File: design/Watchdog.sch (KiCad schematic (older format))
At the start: 25 parts, among them U401 74LV14, U402 74LVC2G00, U403 STWD100xxWY, U404 STWD100xxWY, U405 74AHC157

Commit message: Simplify Watchdog
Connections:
- net IN_CHARGE: now also U402.1; no longer U402.5
- net FC2_WDO: now reaches U404.1 (~WDO)
- net FC2_WDO: now also U402.6; no longer U402.6
- net FC1_WDO: now reaches U403.1 (~WDO)
- net FC1_WDO: now also U402.2; no longer U402.1
- net at R407.1: now also U402.3; no longer U402.7
- new net: U402.5, U402.7
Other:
- moved on the sheet: C406, R401, R407, TP401, U403
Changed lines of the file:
@@
 $Comp
 L CommsCard:74LVC2G00 U402
-U 2 1 5A7B6676
-P 6100 3200
-F 0 "U402" H 6075 3467 50  0000 C CNN
-F 1 "74LVC2G00" H 6075 3376 50  0000 C CNN
-F 2 "Package_SO:VSSOP-8_2.3x2mm_P0.5mm" H 6100 3200 50  0001 C CNN
-F 3 "http://www.ti.com/lit/ds/symlink/sn74lvc2g00.pdf" H 6100 3200 50  0001 C CNN
-F 4 "SN74LVC2G00DCUR" H 6100 3200 50  0001 C CNN "mpn"
-	2    6100 3200
-	1    0    0    -1
-$EndComp
-Wire Wire Line
-	5800 3150 5750 3150
-Wire Wire Line
-	7050 1900 6700 1900
-Wire Wire Line
-	6350 3200 6550 3200
-Wire Wire Line
-	6550 3200 6550 3450
-Wire Wire Line
-	6550 3450 5600 3450
-Wire Wire Line
-	5600 3450 5600 1950
-Wire Wire Line
-	5600 1950 5800 1950
-Wire Wire Line
-	6400 1900 6350 1900
-Wire Wire Line
-	5750 2600 7050 2600
-Wire Wire Line
-	5750 2600 5750 3150
-Wire Wire Line
-	7050 1900 7050 2600
-Wire Wire Line
-	5800 3250 4800 3250
-Wire Wire Line
-	5800 1850 4750 1850
+U 1 1 5A7B6676
+P 6050 1850
+F 0 "U402" H 6025 2117 50  0000 C CNN
+F 1 "74LVC2G00" H 6025 2026 50  0000 C CNN
+F 2 "Package_SO:VSSOP-8_2.3x2mm_P0.5mm" H 6050 1850 50  0001 C CNN
+F 3 "http://www.ti.com/lit/ds/symlink/sn74lvc2g00.pdf" H 6050 1850 50  0001 C CNN
+F 4 "SN74LVC2G00DCUR" H 6050 1850 50  0001 C CNN "mpn"
+	1    6050 1850
+	1    0    0    -1
+$EndComp
+Wire Wire Line
+	7400 1900 7350 1900
+Wire Wire Line
+	7050 1900 7000 1900
+Wire Wire Line
+	7400 1900 7400 2600
 $Comp
 L power:GND #PWR0407
 U 1 1 5A7B7021
-P 4400 2250
-F 0 "#PWR0407" H 4400 2000 50  0001 C CNN
-F 1 "GND" H 4405 2077 50  0000 C CNN
-F 2 "" H 4400 2250 50  0001 C CNN
-F 3 "" H 4400 2250 50  0001 C CNN
-	1    4400 2250
-	1    0    0    -1
-$EndComp
-Wire Wire Line
-	4400 2250 4400 2200
+P 4400 2300
+F 0 "#PWR0407" H 4400 2050 50  0001 C CNN
+F 1 "GND" H 4405 2127 50  0000 C CNN
+F 2 "" H 4400 2300 50  0001 C CNN
+F 3 "" H 4400 2300 50  0001 C CNN
+	1    4400 2300
+	1    0    0    -1
+$EndComp
+Wire Wire Line
+	4400 2300 4400 2250
 $Comp
 L power:GND #PWR0409
@@
 $Comp
 L CommsCard:74LVC2G00 U402
-U 1 1 5A7B74F5
-P 6100 1900
-F 0 "U402" H 6075 2167 50  0000 C CNN
-F 1 "74LVC2G00" H 6075 2076 50  0000 C CNN
-F 2 "Package_SO:VSSOP-8_2.3x2mm_P0.5mm" H 6100 1900 50  0001 C CNN
-F 3 "http://www.ti.com/lit/ds/symlink/sn74lvc2g00.pdf" H 6100 1900 50  0001 C CNN
-F 4 "SN74LVC2G00DCUR" H 6100 1900 50  0001 C CNN "mpn"
-	1    6100 1900
-	1    0    0    -1
-$EndComp
-Wire Wire Line
-	4050 1750 3800 1750
-Text HLabel 3700 1750 0    50   Input ~ 0
+U 2 1 5A7B74F5
+P 6750 1900
+F 0 "U402" H 6725 2167 50  0000 C CNN
+F 1 "74LVC2G00" H 6725 2076 50  0000 C CNN
+F 2 "Package_SO:VSSOP-8_2.3x2mm_P0.5mm" H 6750 1900 50  0001 C CNN
+F 3 "http://www.ti.com/lit/ds/symlink/sn74lvc2g00.pdf" H 6750 1900 50  0001 C CNN
+F 4 "SN74LVC2G00DCUR" H 6750 1900 50  0001 C CNN "mpn"
+	2    6750 1900
+	1    0    0    -1
+$EndComp
+Wire Wire Line
+	4050 1800 3800 1800
+Text HLabel 3700 1800 0    50   Input ~ 0
 FC1_WD
 $Comp
 L Connector_Specialized:Test_Point TP401
 U 1 1 5A7B77EA
-P 3800 1500
-F 0 "TP401" H 3858 1620 50  0000 L CNN
-F 1 "Test_Point" H 3858 1529 50  0000 L CNN
-F 2 "TestPoint:TestPoint_Pad_D1.5mm" H 4000 1500 50  0001 C CNN
-F 3 "~" H 4000 1500 50  0001 C CNN
-F 4 "~" H 3800 1500 50  0001 C CNN "mpn"
-	1    3800 1500
-	1    0    0    -1
-$EndComp
-Wire Wire Line
-	3800 1750 3800 1500
-Connection ~ 3800 1750
-Wire Wire Line
-	3800 1750 3700 1750
+P 3800 1550
+F 0 "TP401" H 3858 1670 50  0000 L CNN
+F 1 "Test_Point" H 3858 1579 50  0000 L CNN
+F 2 "TestPoint:TestPoint_Pad_D1.5mm" H 4000 1550 50  0001 C CNN
+F 3 "~" H 4000 1550 50  0001 C CNN
+F 4 "~" H 3800 1550 50  0001 C CNN "mpn"
+	1    3800 1550
+	1    0    0    -1
+$EndComp
+Wire Wire Line
+	3800 1800 3800 1550
+Connection ~ 3800 1800
+Wire Wire Line
+	3800 1800 3700 1800
 Wire Wire Line
 	4100 3150 3850 3150
@@
 ~FC2_PWREN
 Wire Wire Line
-	3050 1950 3050 1900
-Wire Wire Line
-	3050 1950 4050 1950
+	3050 2000 3050 1950
+Wire Wire Line
+	3050 2000 4050 2000
 $Comp
 L power:+3V3 #PWR0401
 U 1 1 5A7B889A
-P 3050 1550
-F 0 "#PWR0401" H 3050 1400 50  0001 C CNN
-F 1 "+3V3" H 3065 1723 50  0000 C CNN
-F 2 "" H 3050 1550 50  0001 C CNN
-F 3 "" H 3050 1550 50  0001 C CNN
-	1    3050 1550
-	1    0    0    -1
-$EndComp
-Wire Wire Line
-	3050 1600 3050 1550
-Text HLabel 3050 1950 0    50   Input ~ 0
+P 3050 1600
+F 0 "#PWR0401" H 3050 1450 50  0001 C CNN
+F 1 "+3V3" H 3065 1773 50  0000 C CNN
+F 2 "" H 3050 1600 50  0001 C CNN
+F 3 "" H 3050 1600 50  0001 C CNN
+	1    3050 1600
+	1    0    0    -1
+$EndComp
+Wire Wire Line
+	3050 1650 3050 1600
+Text HLabel 3050 2000 0    50   Input ~ 0
 ~FC1_PWREN
 $Comp
@@
 L power:+3V3 #PWR0406
 U 1 1 5A7B9130
-P 4400 1500
-F 0 "#PWR0406" H 4400 1350 50  0001 C CNN
-F 1 "+3V3" H 4415 1673 50  0000 C CNN
-F 2 "" H 4400 1500 50  0001 C CNN
-F 3 "" H 4400 1500 50  0001 C CNN
-	1    4400 1500
+P 4400 1550
+F 0 "#PWR0406" H 4400 1400 50  0001 C CNN
+F 1 "+3V3" H 4415 1723 50  0000 C CNN
+F 2 "" H 4400 1550 50  0001 C CNN
+F 3 "" H 4400 1550 50  0001 C CNN
+	1    4400 1550
 	1    0    0    -1
 $EndComp
@@
 	1    0    0    -1
 $EndComp
-Connection ~ 7050 2600
+Connection ~ 7400 2600
 $Comp
 L power:+3V3 #PWR0412
@@
 L CommsCard:STWD100xxWY U403
 U 1 1 5A7BE12B
-P 4400 1850
-F 0 "U403" H 4791 1896 50  0000 L CNN
-F 1 "STWD100xxWY" H 4791 1805 50  0000 L CNN
-F 2 "Package_TO_SOT_SMD:SOT-353_SC-70-5" H 4450 2050 50  0001 C CNN
-F 3 "http://www.st.com/content/ccc/resource/technical/document/datasheet/06/6a/b3/83/9a/c7/4f/22/CD00176077.pdf/files/CD00176077.pdf/jcr:content/translations/en.CD00176077.pdf" H 4550 2150 50  0001 C CNN
-F 4 "STWD100PYW83F" H 4400 1850 50  0001 C CNN "mpn"
-	1    4400 1850
+P 4400 1900
+F 0 "U403" H 4791 1946 50  0000 L CNN
+F 1 "STWD100xxWY" H 4791 1855 50  0000 L CNN
+F 2 "Package_TO_SOT_SMD:SOT-353_SC-70-5" H 4450 2100 50  0001 C CNN
+F 3 "http://www.st.com/content/ccc/resource/technical/document/datasheet/06/6a/b3/83/9a/c7/4f/22/CD00176077.pdf/files/CD00176077.pdf/jcr:content/translations/en.CD00176077.pdf" H 4550 2200 50  0001 C CNN
+F 4 "STWD100PYW83F" H 4400 1900 50  0001 C CNN "mpn"
+	1    4400 1900
 	1    0    0    -1
 $EndComp
@@
 Connection ~ 8650 3050
 Wire Wire Line
-	7050 2600 7050 2850
-Wire Wire Line
-	7050 2850 7300 2850
-Text HLabel 7300 2850 2    50   Output ~ 0
+	7400 2600 7400 2850
+Wire Wire Line
+	7400 2850 7650 2850
+Text HLabel 7650 2850 2    50   Output ~ 0
 IN_CHARGE
 $Comp
@@
 L Device:R R407
 U 1 1 5A836CA1
-P 6550 1900
-F 0 "R407" H 6480 1854 50  0000 R CNN
-F 1 "10k" H 6480 1945 50  0000 R CNN
-F 2 "Resistor_SMD:R_0603_1608Metric" V 6480 1900 50  0001 C CNN
-F 3 "http://www.te.com/commerce/DocumentDelivery/DDEController?Action=srchrtrv&DocNm=1773204&DocType=DS&DocLang=English" H 6550 1900 50  0001 C CNN
-F 4 "CRG0603J10K" H 6550 1900 50  0001 C CNN "mpn"
-	1    6550 1900
+P 7200 1900
+F 0 "R407" H 7130 1854 50  0000 R CNN
+F 1 "10k" H 7130 1945 50  0000 R CNN
+F 2 "Resistor_SMD:R_0603_1608Metric" V 7130 1900 50  0001 C CNN
+F 3 "http://www.te.com/commerce/DocumentDelivery/DDEController?Action=srchrtrv&DocNm=1773204&DocType=DS&DocLang=English" H 7200 1900 50  0001 C CNN
+F 4 "CRG0603J10K" H 7200 1900 50  0001 C CNN "mpn"
+	1    7200 1900
 	0    -1   1    0
 $EndComp
@@
 L Device:R R401
 U 1 1 5A83892F
-P 3050 1750
-F 0 "R401" H 2980 1704 50  0000 R CNN
-F 1 "10k" H 2980 1795 50  0000 R CNN
-F 2 "Resistor_SMD:R_0603_1608Metric" V 2980 1750 50  0001 C CNN
-F 3 "http://www.te.com/commerce/DocumentDelivery/DDEController?Action=srchrtrv&DocNm=1773204&DocType=DS&DocLang=English" H 3050 1750 50  0001 C CNN
-F 4 "CRG0603J10K" H 3050 1750 50  0001 C CNN "mpn"
-	1    3050 1750
+P 3050 1800
+F 0 "R401" H 2980 1754 50  0000 R CNN
+F 1 "10k" H 2980 1845 50  0000 R CNN
+F 2 "Resistor_SMD:R_0603_1608Metric" V 2980 1800 50  0001 C CNN
+F 3 "http://www.te.com/commerce/DocumentDelivery/DDEController?Action=srchrtrv&DocNm=1773204&DocType=DS&DocLang=English" H 3050 1800 50  0001 C CNN
+F 4 "CRG0603J10K" H 3050 1800 50  0001 C CNN "mpn"
+	1    3050 1800
 	1    0    0    1
 $EndComp
@@
 L Device:C C406
 U 1 1 5A887245
-P 7050 3150
-F 0 "C406" H 7165 3196 50  0000 L CNN
-F 1 "0u1F" H 7165 3105 50  0000 L CNN
-F 2 "Capacitor_SMD:C_0603_1608Metric" H 7088 3000 50  0001 C CNN
-F 3 "http://www.samsungsem.com/kr/support/product-search/mlcc/CL10B104KO8WPNC.jsp" H 7050 3150 50  0001 C CNN
-F 4 "CL10B104KO8WPNC" H 7050 3150 50  0001 C CNN "mpn"
-	1    7050 3150
+P 7400 3150
+F 0 "C406" H 7515 3196 50  0000 L CNN
+F 1 "0u1F" H 7515 3105 50  0000 L CNN
+F 2 "Capacitor_SMD:C_0603_1608Metric" H 7438 3000 50  0001 C CNN
+F 3 "http://www.samsungsem.com/kr/support/product-search/mlcc/CL10B104KO8WPNC.jsp" H 7400 3150 50  0001 C CNN
+F 4 "CL10B104KO8WPNC" H 7400 3150 50  0001 C CNN "mpn"
+	1    7400 3150
 	1    0    0    -1
 $EndComp
@@
 L power:GND #PWR0411
 U 1 1 5A88736C
-P 7050 3350
-F 0 "#PWR0411" H 7050 3100 50  0001 C CNN
-F 1 "GND" H 7055 3177 50  0000 C CNN
-F 2 "" H 7050 3350 50  0001 C CNN
-F 3 "" H 7050 3350 50  0001 C CNN
-	1    7050 3350
-	1    0    0    -1
-$EndComp
-Wire Wire Line
-	7050 3350 7050 3300
-Connection ~ 7050 2850
-Wire Wire Line
-	7050 2850 7050 3000
+P 7400 3350
+F 0 "#PWR0411" H 7400 3100 50  0001 C CNN
+F 1 "GND" H 7405 3177 50  0000 C CNN
+F 2 "" H 7400 3350 50  0001 C CNN
+F 3 "" H 7400 3350 50  0001 C CNN
+	1    7400 3350
+	1    0    0    -1
+$EndComp
+Wire Wire Line
+	7400 3350 7400 3300
+Connection ~ 7400 2850
+Wire Wire Line
+	7400 2850 7400 3000
 Connection ~ 9900 5600
 Wire Wire Line
-	7050 2600 8250 2600
+	7400 2600 8250 2600
 Wire Wire Line
 	9900 5600 9900 5500
+Text Label 5150 3250 0    50   ~ 0
+FC2_WDO
+Text Label 5200 1900 0    50   ~ 0
+FC1_WDO
+Wire Wire Line
+	4750 1900 5750 1900
+Wire Wire Line
+	7400 1900 7400 1400
+Wire Wire Line
+	7400 1400 5650 1400
+Wire Wire Line
+	5650 1400 5650 1800
+Wire Wire Line
+	5650 1800 5750 1800
+Connection ~ 7400 1900
+Wire Wire Line
+	6450 1850 6300 1850
+Wire Wire Line
+	6350 3250 6350 1950
+Wire Wire Line
+	4800 3250 6350 3250
+Wire Wire Line
+	6350 1950 6450 1950
+Connection ~ 6150 2800
 $EndSCHEMATC

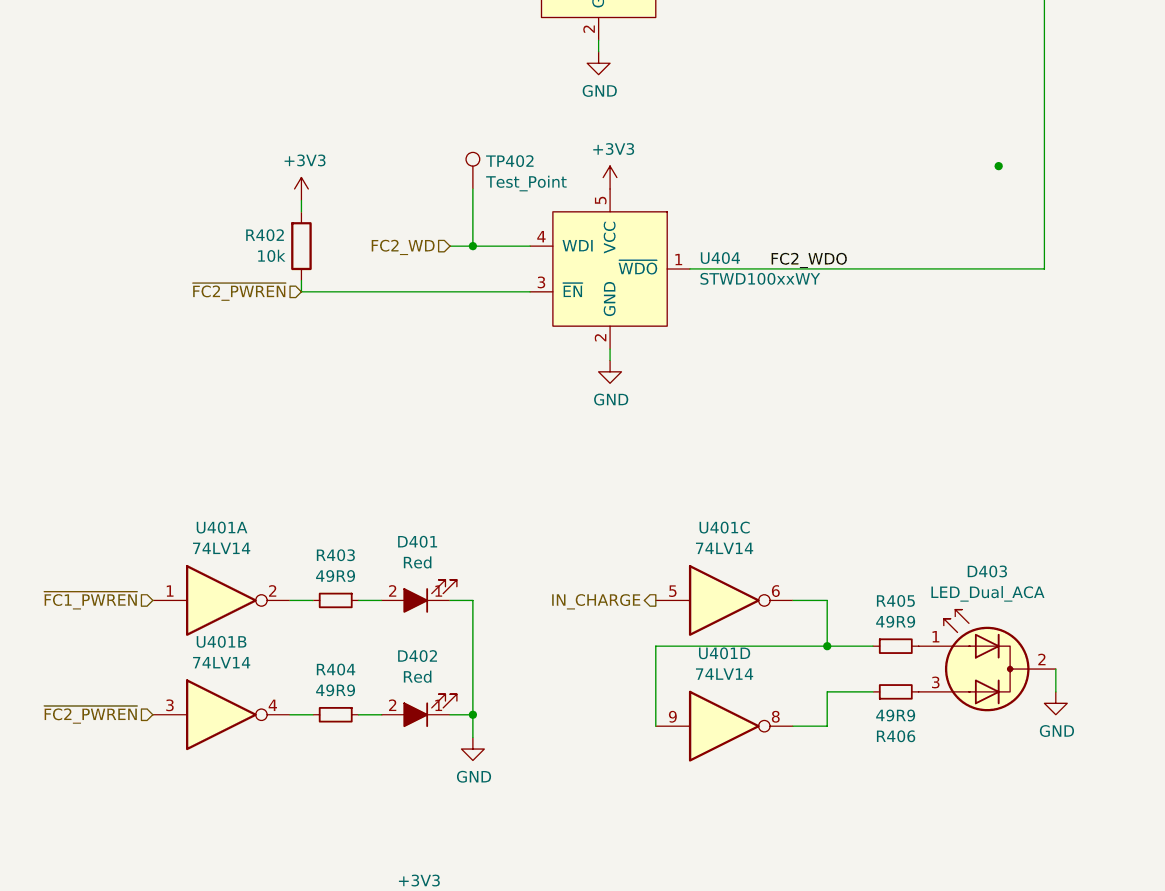
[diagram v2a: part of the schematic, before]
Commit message: Layout additional watchdog
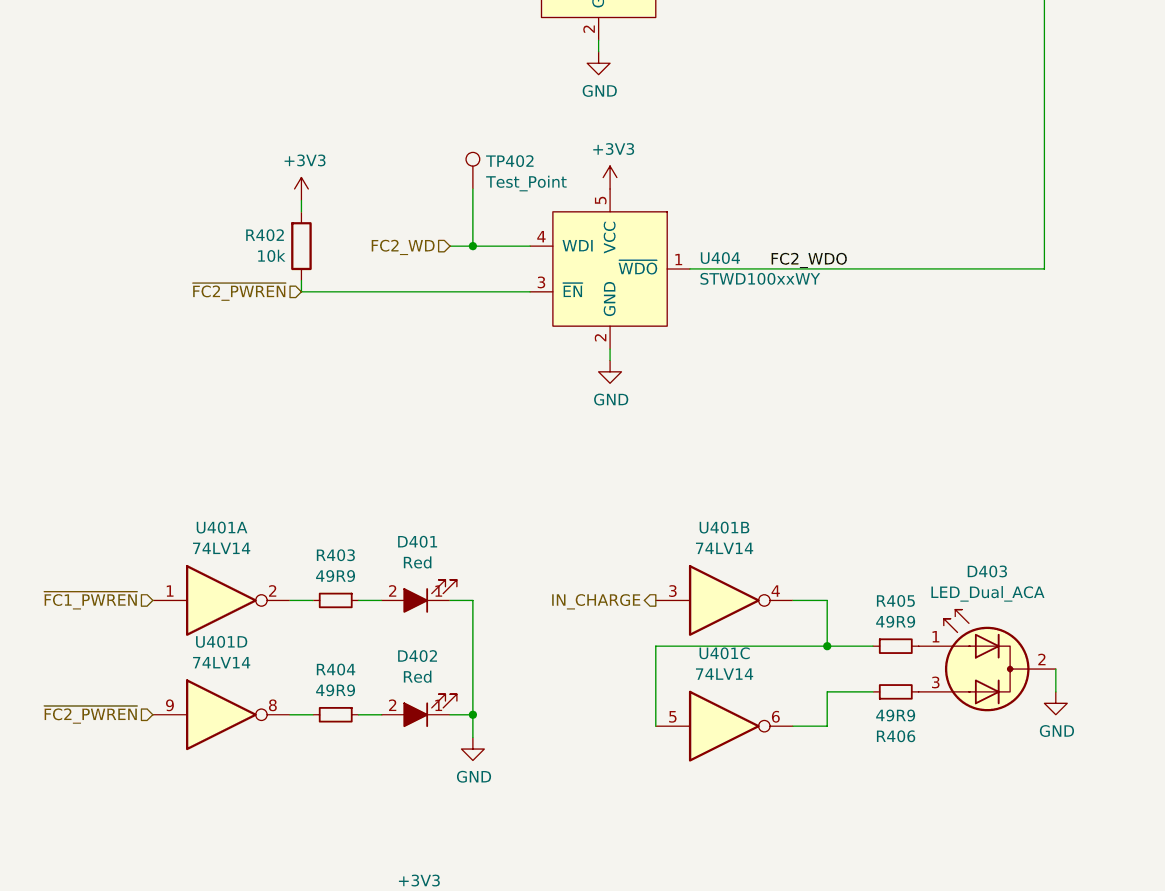
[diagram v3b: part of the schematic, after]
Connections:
- net IN_CHARGE: now also U401.3; no longer U401.5
- net ~FC2_PWREN: now also U401.9; no longer U401.3
- net at U401.4: now also R405.1, U401.5; no longer R404.2
- net at R406.1: now also U401.6; no longer U401.8
- new net: R404.2, U401.8
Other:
- moved on the sheet: U401B, U401C, U401D
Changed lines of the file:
@@
 L Logic_74xx:74HC04 U401
 U 3 1 5A8462FD
-P 4950 4700
-F 0 "U401" H 4950 5017 50  0000 C CNN
-F 1 "74LV14" H 4950 4926 50  0000 C CNN
-F 2 "Package_SO:TSSOP-14_4.4x5mm_P0.65mm" H 4950 4700 50  0001 C CNN
-F 3 "http://www.ti.com/lit/ds/symlink/sn74lv14a.pdf" H 4950 4700 50  0001 C CNN
-F 4 "SN74LV14APWR" H 4950 4700 50  0001 C CNN "mpn"
-	3    4950 4700
+P 4950 5250
+F 0 "U401" H 4950 5567 50  0000 C CNN
+F 1 "74LV14" H 4950 5476 50  0000 C CNN
+F 2 "Package_SO:TSSOP-14_4.4x5mm_P0.65mm" H 4950 5250 50  0001 C CNN
+F 3 "http://www.ti.com/lit/ds/symlink/sn74lv14a.pdf" H 4950 5250 50  0001 C CNN
+F 4 "SN74LV14APWR" H 4950 5250 50  0001 C CNN "mpn"
+	3    4950 5250
 	1    0    0    -1
 $EndComp
@@
 L Logic_74xx:74HC04 U401
 U 4 1 5A85B128
-P 4950 5250
-F 0 "U401" H 4950 5567 50  0000 C CNN
-F 1 "74LV14" H 4950 5476 50  0000 C CNN
-F 2 "Package_SO:TSSOP-14_4.4x5mm_P0.65mm" H 4950 5250 50  0001 C CNN
-F 3 "http://www.ti.com/lit/ds/symlink/sn74lv14a.pdf" H 4950 5250 50  0001 C CNN
-F 4 "SN74LV14APWR" H 4950 5250 50  0001 C CNN "mpn"
-	4    4950 5250
-	1    0    0    -1
-$EndComp
-$Comp
-L Logic_74xx:74HC04 U401
-U 2 1 5A85B182
 P 2750 5200
 F 0 "U401" H 2750 5517 50  0000 C CNN
@@
 F 3 "http://www.ti.com/lit/ds/symlink/sn74lv14a.pdf" H 2750 5200 50  0001 C CNN
 F 4 "SN74LV14APWR" H 2750 5200 50  0001 C CNN "mpn"
-	2    2750 5200
+	4    2750 5200
+	1    0    0    -1
+$EndComp
+$Comp
+L Logic_74xx:74HC04 U401
+U 2 1 5A85B182
+P 4950 4700
+F 0 "U401" H 4950 5017 50  0000 C CNN
+F 1 "74LV14" H 4950 4926 50  0000 C CNN
+F 2 "Package_SO:TSSOP-14_4.4x5mm_P0.65mm" H 4950 4700 50  0001 C CNN
+F 3 "http://www.ti.com/lit/ds/symlink/sn74lv14a.pdf" H 4950 4700 50  0001 C CNN
+F 4 "SN74LV14APWR" H 4950 4700 50  0001 C CNN "mpn"
+	2    4950 4700
 	1    0    0    -1
 $EndComp
@@
 Wire Wire Line
 	6350 1950 6450 1950
-Connection ~ 6150 2800
 $EndSCHEMATC

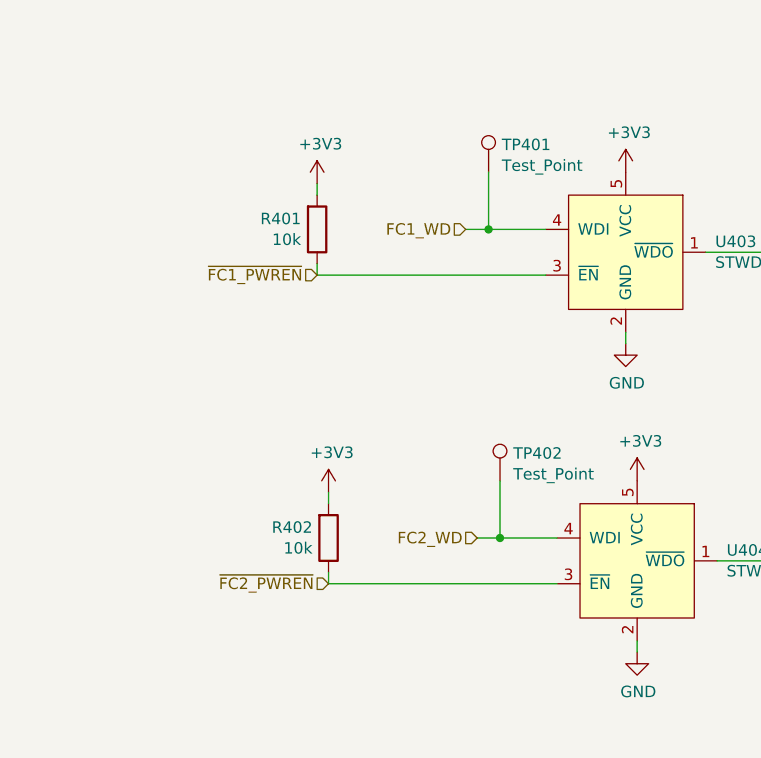
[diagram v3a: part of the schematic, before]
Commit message: Further LOS updates.  Compressing space
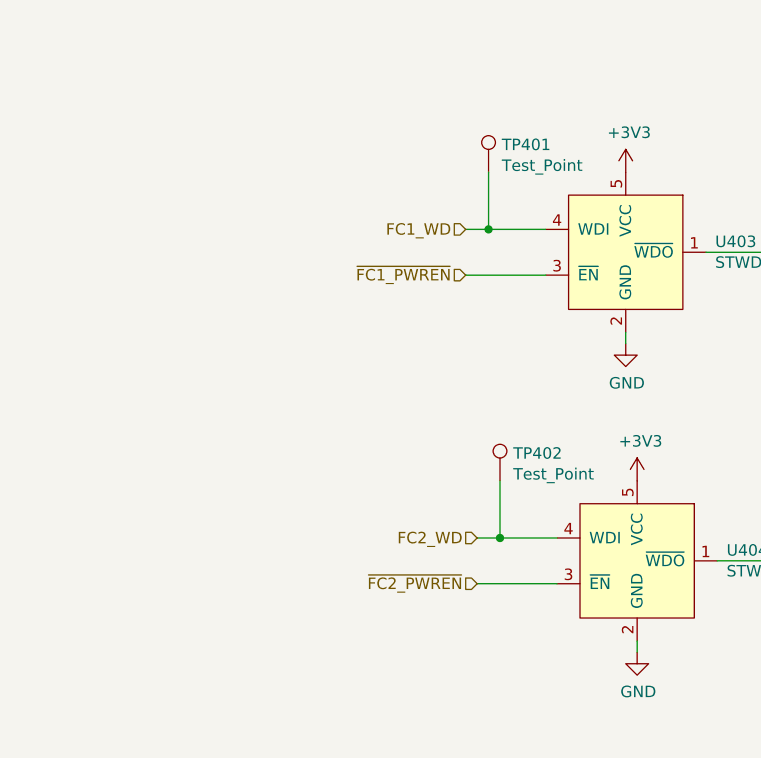
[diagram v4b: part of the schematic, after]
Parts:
- removed R401, R402: 10k, Resistor_SMD:R_0603_1608Metric, symbol Device:R
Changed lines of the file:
@@
 	3850 3150 3750 3150
 Wire Wire Line
-	3100 3350 3100 3300
-Wire Wire Line
-	3100 3350 4100 3350
-$Comp
-L power:+3V3 #PWR0402
-U 1 1 5A7B80F0
-P 3100 2950
-F 0 "#PWR0402" H 3100 2800 50  0001 C CNN
-F 1 "+3V3" H 3115 3123 50  0000 C CNN
-F 2 "" H 3100 2950 50  0001 C CNN
-F 3 "" H 3100 2950 50  0001 C CNN
-	1    3100 2950
-	1    0    0    -1
-$EndComp
-Wire Wire Line
-	3100 3000 3100 2950
-Text HLabel 3100 3350 0    50   Input ~ 0
+	3750 3350 4100 3350
+Text HLabel 3750 3350 0    50   Input ~ 0
 ~FC2_PWREN
 Wire Wire Line
-	3050 2000 3050 1950
-Wire Wire Line
-	3050 2000 4050 2000
-$Comp
-L power:+3V3 #PWR0401
-U 1 1 5A7B889A
-P 3050 1600
-F 0 "#PWR0401" H 3050 1450 50  0001 C CNN
-F 1 "+3V3" H 3065 1773 50  0000 C CNN
-F 2 "" H 3050 1600 50  0001 C CNN
-F 3 "" H 3050 1600 50  0001 C CNN
-	1    3050 1600
-	1    0    0    -1
-$EndComp
-Wire Wire Line
-	3050 1650 3050 1600
-Text HLabel 3050 2000 0    50   Input ~ 0
+	3700 2000 4050 2000
+Text HLabel 3700 2000 0    50   Input ~ 0
 ~FC1_PWREN
 $Comp
@@
 $EndComp
 $Comp
-L Device:R R401
-U 1 1 5A83892F
-P 3050 1800
-F 0 "R401" H 2980 1754 50  0000 R CNN
-F 1 "10k" H 2980 1845 50  0000 R CNN
-F 2 "Resistor_SMD:R_0603_1608Metric" V 2980 1800 50  0001 C CNN
-F 3 "http://www.te.com/commerce/DocumentDelivery/DDEController?Action=srchrtrv&DocNm=1773204&DocType=DS&DocLang=English" H 3050 1800 50  0001 C CNN
-F 4 "CRG0603J10K" H 3050 1800 50  0001 C CNN "mpn"
-	1    3050 1800
-	1    0    0    1
-$EndComp
-$Comp
-L Device:R R402
-U 1 1 5A839815
-P 3100 3150
-F 0 "R402" H 3030 3104 50  0000 R CNN
-F 1 "10k" H 3030 3195 50  0000 R CNN
-F 2 "Resistor_SMD:R_0603_1608Metric" V 3030 3150 50  0001 C CNN
-F 3 "http://www.te.com/commerce/DocumentDelivery/DDEController?Action=srchrtrv&DocNm=1773204&DocType=DS&DocLang=English" H 3100 3150 50  0001 C CNN
-F 4 "CRG0603J10K" H 3100 3150 50  0001 C CNN "mpn"
-	1    3100 3150
-	1    0    0    1
-$EndComp
-$Comp

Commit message: Minimizing space in design
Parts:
- D403: footprint LED_THT:LED_D8.0mm-3 -> LEDs:WP130WDT
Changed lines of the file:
@@
 F 0 "D403" H 6100 5425 50  0000 C CNN
 F 1 "LED_Dual_ACA" H 6100 5334 50  0000 C CNN
-F 2 "LED_THT:LED_D8.0mm-3" H 6100 5000 50  0001 C CNN
+F 2 "LEDs:WP130WDT" H 6100 5000 50  0001 C CNN
 F 3 "http://www.kingbrightusa.com/images/catalog/SPEC/WP130WDT-EYW.pdf" H 6100 5000 50  0001 C CNN
 F 4 "WP130WDT/EYW" H 6100 5000 50  0001 C CNN "mpn"
